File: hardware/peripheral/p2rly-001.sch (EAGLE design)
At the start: 4 parts, among them J4 RLY

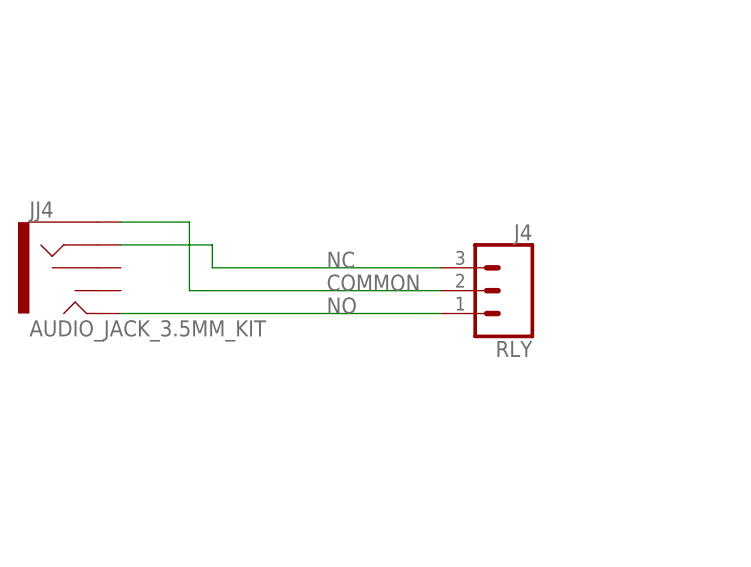
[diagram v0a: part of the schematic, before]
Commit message: Fixed polarity.
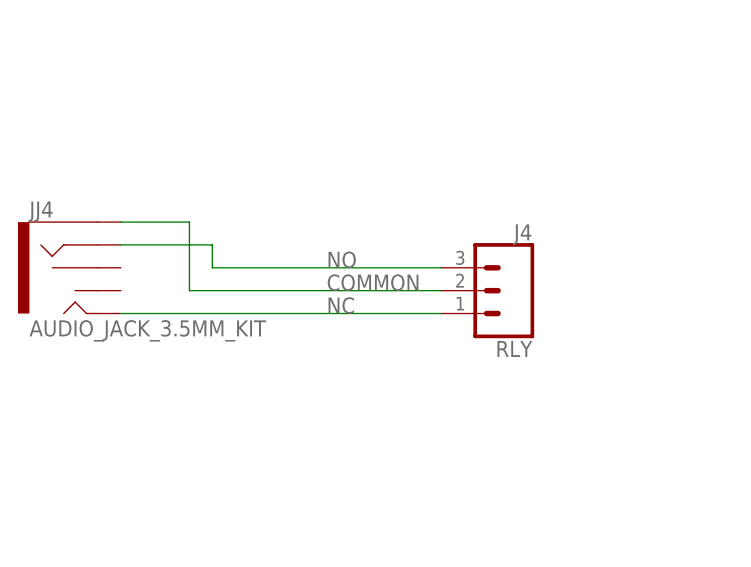
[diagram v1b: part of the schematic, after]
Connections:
- net NC: now also J4.1, JJ4.TIP; no longer J4.3, JJ4.RING
- net NO: now also J4.3, JJ4.RING; no longer J4.1, JJ4.TIP
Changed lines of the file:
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@@
 </busses>
 <nets>
-<net name="NO" class="0">
-<segment>
-<pinref part="JJ4" gate="G$1" pin="TIP"/>
-<pinref part="J4" gate="J$1" pin="1"/>
-<wire x1="35.56" y1="119.38" x2="71.12" y2="119.38" width="0.1524" layer="91"/>
-<label x="58.42" y="119.38" size="1.778" layer="95"/>
-</segment>
-</net>
 <net name="COMMON" class="0">
 <segment>
@@
 <net name="NC" class="0">
 <segment>
+<pinref part="JJ4" gate="G$1" pin="TIP"/>
+<pinref part="J4" gate="J$1" pin="1"/>
+<wire x1="35.56" y1="119.38" x2="71.12" y2="119.38" width="0.1524" layer="91"/>
+<label x="58.42" y="119.38" size="1.778" layer="95"/>
+</segment>
+</net>
+<net name="NO" class="0">
+<segment>
 <pinref part="JJ4" gate="G$1" pin="RING"/>
